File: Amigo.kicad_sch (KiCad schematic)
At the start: 0 parts

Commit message: Power section complete
Schematic Power section
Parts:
- added C1, C2: C, symbol Device:C
- added J1: USB_C_Receptacle_USB2.0_16P, symbol Connector:USB_C_Receptacle_USB2.0_16P
- added J2: Conn_01x02, symbol Connector_Generic:Conn_01x02
- added R1, R2: 5.1k, symbol Device:R
- added R3: 1.2k, symbol Device:R
- added R4, R5: 100k, symbol Device:R
- added U1: TP4056-42-ESOP8, Package_SO:SOIC-8-1EP_3.9x4.9mm_P1.27mm_EP2.41x3.3mm_ThermalVias, symbol Battery_Management:TP4056-42-ESOP8
- added U2: AP2112K-3.3, Package_TO_SOT_SMD:SOT-23-5, symbol Regulator_Linear:AP2112K-3.3
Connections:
- new net +3V3: C2.1, U2.5 (VOUT)
- new net BAT+: C1.1, J2.1 (Pin_1), R4.1, U1.5 (BAT), U2.1 (VIN), U2.3 (EN)
- new net BAT_SENSE: R4.2, R5.1
- new net GND: C1.2, C2.2, J1.A1 (GND), J1.A12 (GND), J1.B1 (GND), J1.B12 (GND), J1.SH (SHIELD), J2.2 (Pin_2), R1.2, R2.2, R3.2, R5.2, U2.2 (GND)
- new net TP4_PROG: R3.1, U1.2 (PROG)
- new net USB_CC1: J1.A5 (CC1), R1.1
- new net USB_CC2: J1.B5 (CC2), R2.1
- new net VBUS_5V: J1.A4 (VBUS), J1.A9 (VBUS), J1.B4 (VBUS), J1.B9 (VBUS), U1.4 (V_{CC})

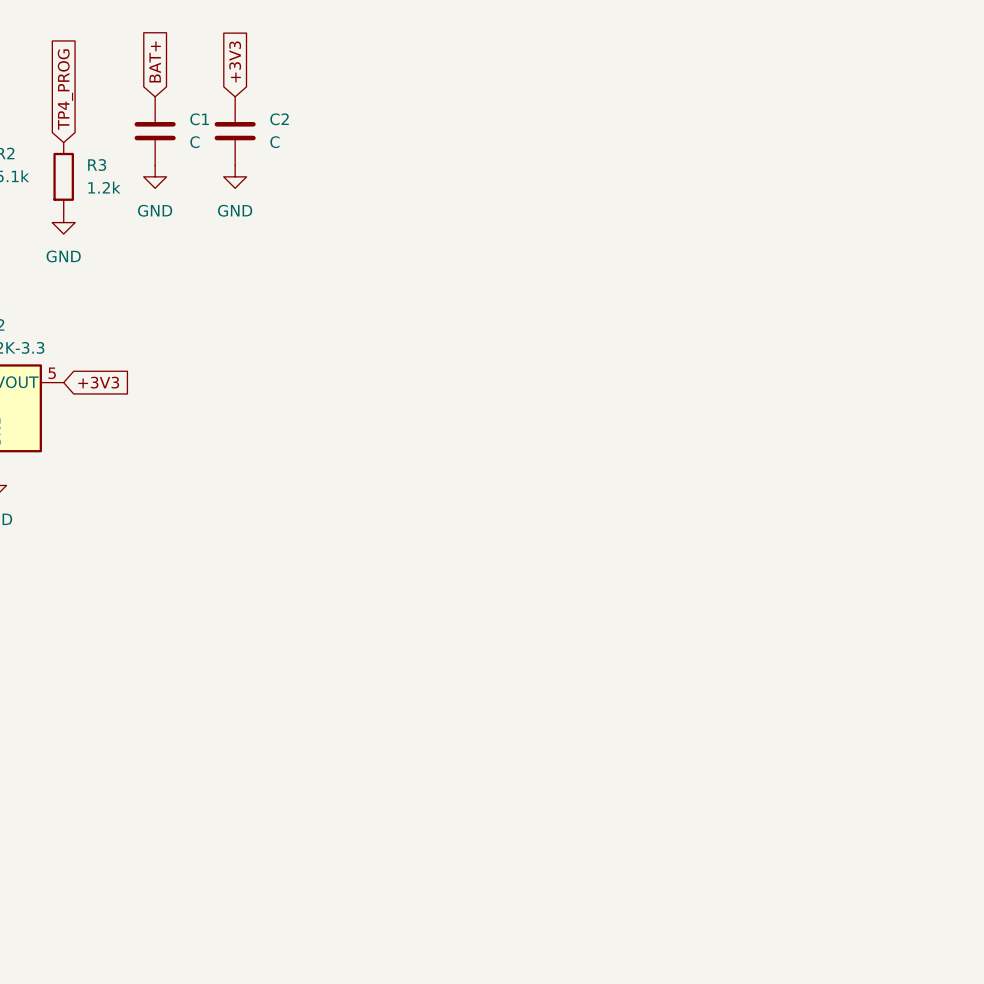
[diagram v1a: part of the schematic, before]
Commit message: Wired up ESP board with all the stuff
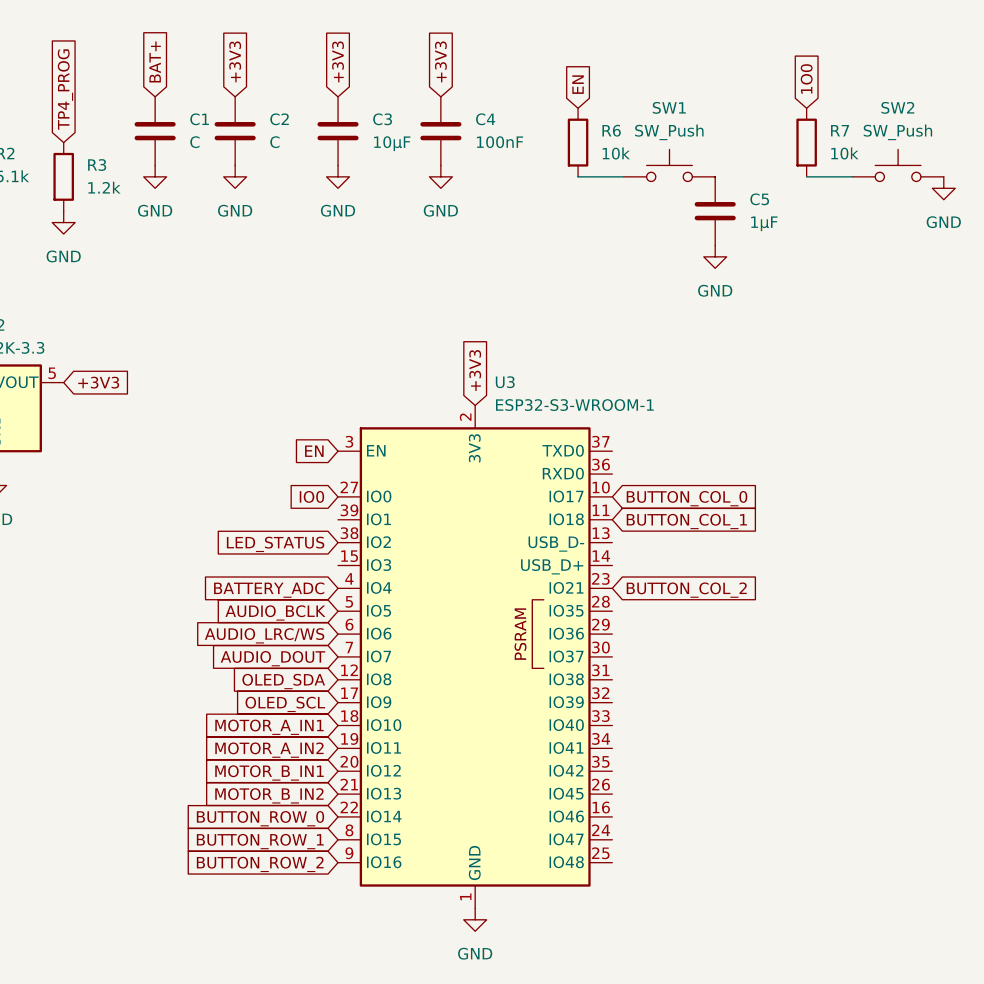
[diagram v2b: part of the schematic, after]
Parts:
- added C3: 10µF, symbol Device:C
- added C4: 100nF, symbol Device:C
- added C5: 1µF, symbol Device:C
- added R6, R7: 10k, symbol Device:R
- added SW1, SW2: SW_Push, symbol Switch:SW_Push
- added U3: ESP32-S3-WROOM-1, RF_Module:ESP32-S3-WROOM-1, symbol RF_Module:ESP32-S3-WROOM-1
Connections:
- net +3V3: now also C3.1, C4.1, U3.2 (3V3)
- net GND: now also C3.2, C4.2, C5.2, SW2.2, U3.1 (GND), U3.40 (GND), U3.41 (GND)
- new net: R6.2, SW1.1
- new net: C5.1, SW1.2
- new net: R7.2, SW2.1
- new net 1O0: R7.1
- new net AUDIO_BCLK: U3.5 (IO5)
- new net AUDIO_DOUT: U3.7 (IO7)
- new net AUDIO_LRC/WS: U3.6 (IO6)
- new net BATTERY_ADC: U3.4 (IO4)
- new net BUTTON_COL_0: U3.10 (IO17)
- new net BUTTON_COL_1: U3.11 (IO18)
- new net BUTTON_COL_2: U3.23 (IO21)
- new net BUTTON_ROW_0: U3.22 (IO14)
- new net BUTTON_ROW_1: U3.8 (IO15)
- new net BUTTON_ROW_2: U3.9 (IO16)
- new net EN: R6.1, U3.3 (EN)
- new net IO0: U3.27 (IO0)
- new net LED_STATUS: U3.38 (IO2)
- new net MOTOR_A_IN1: U3.18 (IO10)
- new net MOTOR_A_IN2: U3.19 (IO11)
- new net MOTOR_B_IN1: U3.20 (IO12)
- new net MOTOR_B_IN2: U3.21 (IO13)
- new net OLED_SCL: U3.17 (IO9)
- new net OLED_SDA: U3.12 (IO8)

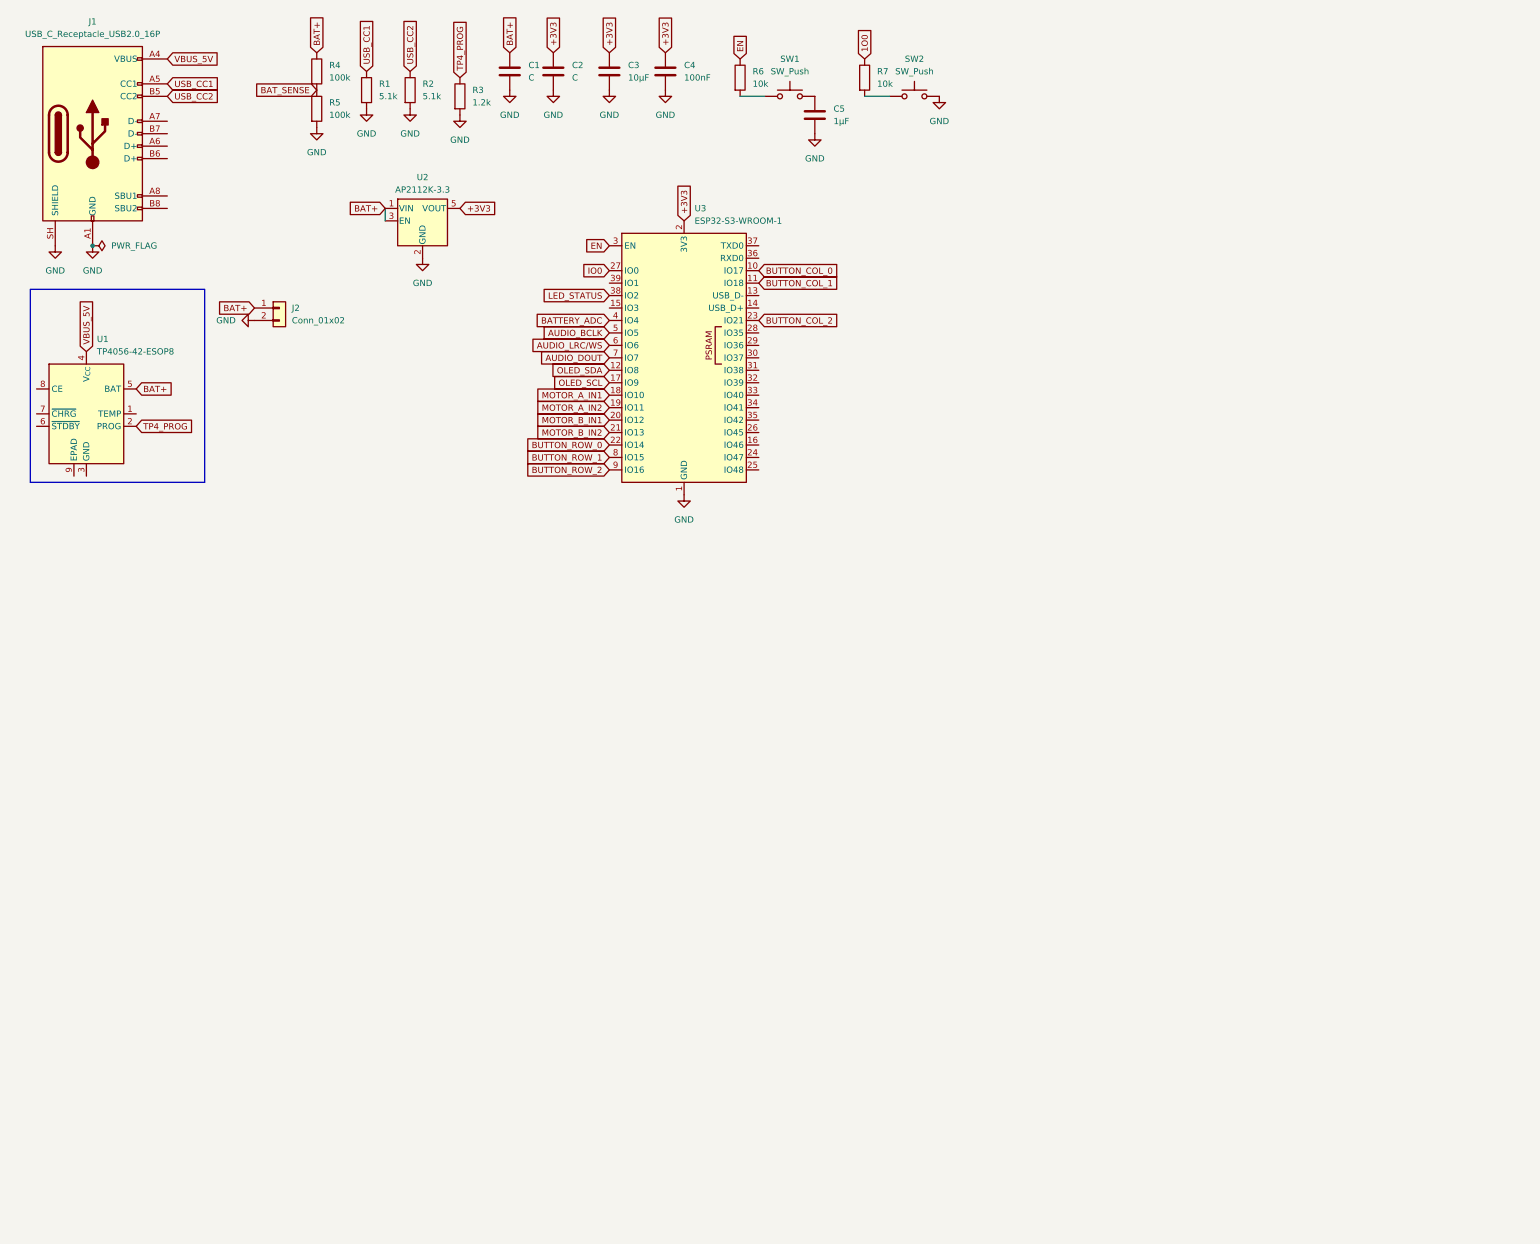
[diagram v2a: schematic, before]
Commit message: Finished wiring audio amp in schematic
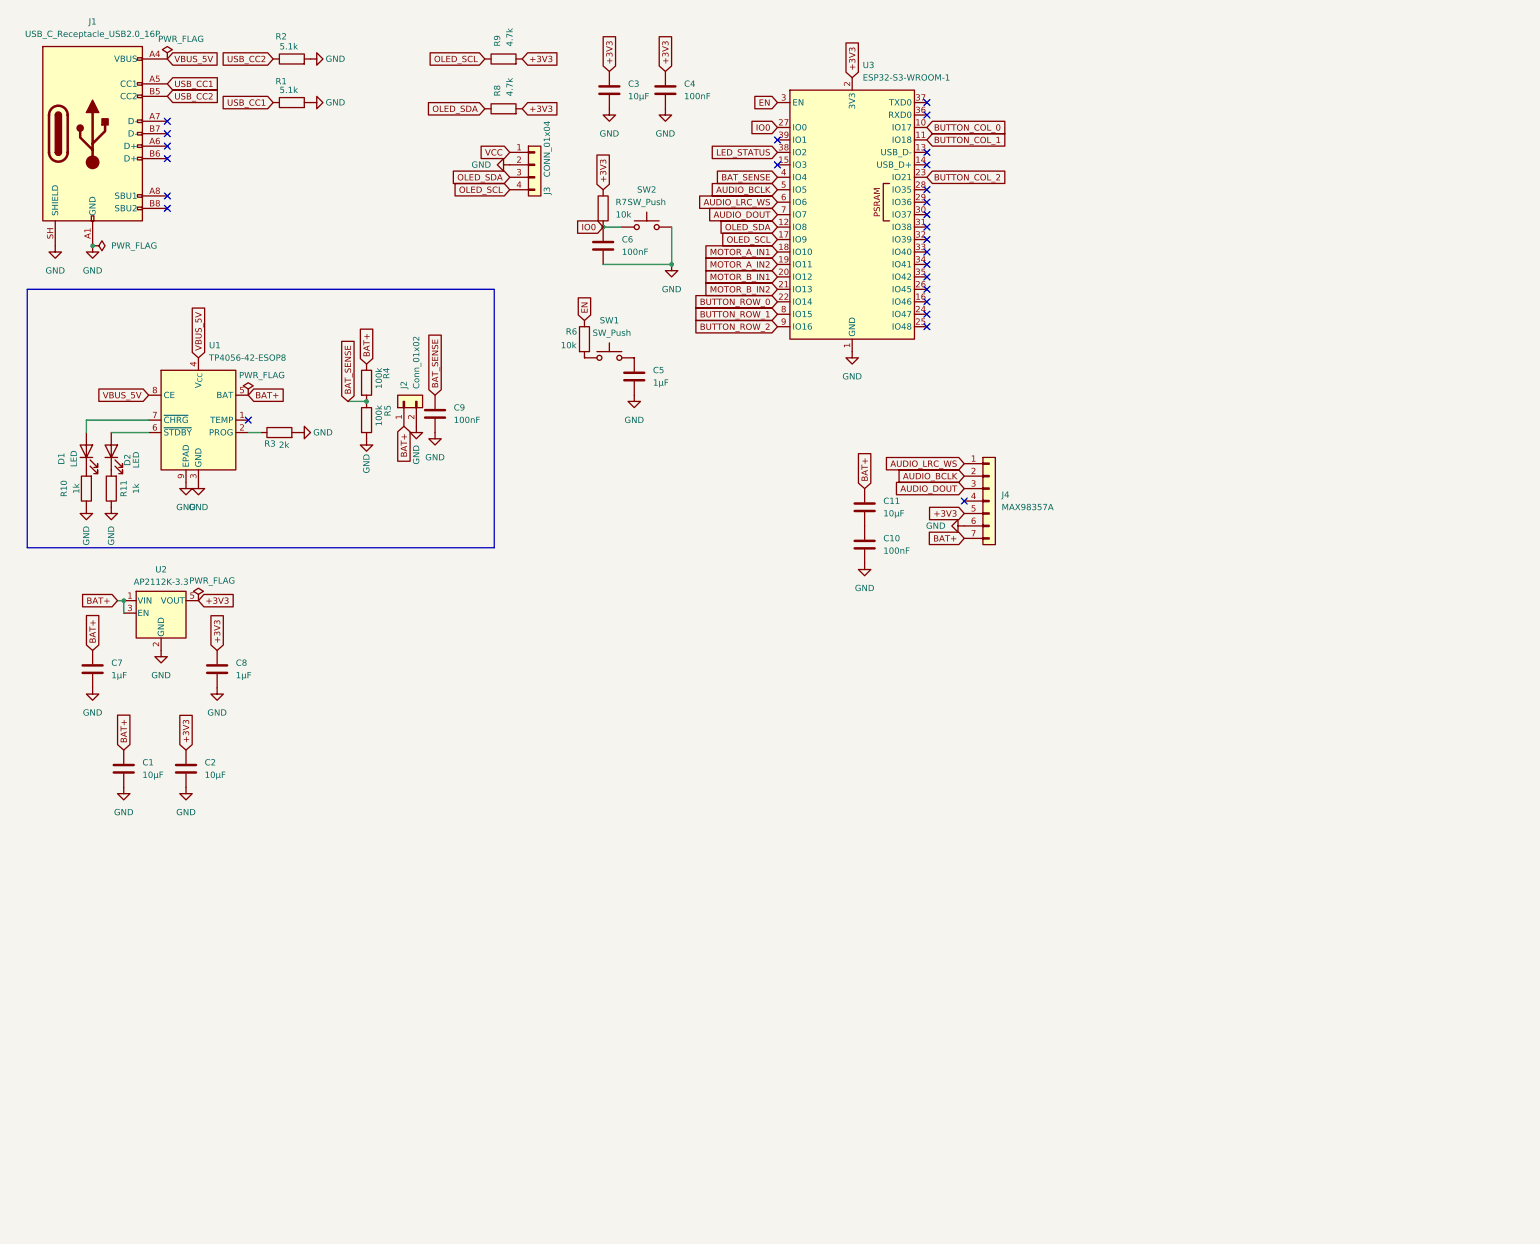
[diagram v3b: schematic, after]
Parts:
- added C10, C6, C9: 100nF, symbol Device:C
- added C11: 10µF, symbol Device:C
- added C7, C8: 1µF, symbol Device:C
- added D1, D2: LED, symbol Device:LED
- added J3: CONN_01x04, symbol Connector_Generic:Conn_01x04
- added J4: MAX98357A, symbol Connector_Generic:Conn_01x07
- added R10, R11: 1k, symbol Device:R
- added R8, R9: 4.7k, symbol Device:R
- C1, C2: value C -> 10µF
- R3: value 1.2k -> 2k
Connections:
- net 1O0 is gone; now on net +3V3: R7.1
- net BATTERY_ADC is gone; now on net BAT_SENSE: U3.4 (IO4)
- net +3V3: now also C8.1, J4.5 (Pin_5), R8.2, R9.2
- net AUDIO_BCLK: now also J4.2 (Pin_2)
- net AUDIO_DOUT: now also J4.3 (Pin_3)
- net BAT+: now also C11.1, C7.1, J4.7 (Pin_7)
- net BAT_SENSE: now also C9.1
- net GND: now also U1.3 (GND), U1.9 (EPAD), C10.2, C6.2, C7.2, C8.2, C9.2, J3.2 (Pin_2), J4.6 (Pin_6), R10.1, R11.1
- net IO0: now also R7.2, SW2.1, C6.1
- net OLED_SCL: now also J3.4 (Pin_4), R9.1
- net OLED_SDA: now also J3.3 (Pin_3), R8.1
- net VBUS_5V: now also U1.8 (CE)
- net at U1.6 (~{STDBY}): now also D2.2 (A)
- net at U1.7 (~{CHRG}): now also D1.2 (A)
- net AUDIO_LRC/WS renamed AUDIO_LRC_WS
- net AUDIO_LRC_WS: now also J4.1 (Pin_1)
- net TP4_PROG: no longer names the net of R3.1, U1.2 (PROG)
- new net: D1.1 (K), R10.2
- new net: D2.1 (K), R11.2
- new net: C10.1, C11.2
- new net VCC: J3.1 (Pin_1)
- no-connect marks 0 -> 26
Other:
- moved on the sheet: C1, C2, C3, C4, C5, J2, R1, R2, R3, R4, R5, R6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

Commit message: Finished wiring motor controller in schematic
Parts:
- added C12: 100nF, symbol Device:C
- added C13: 10µF, symbol Device:C
- added J5: DRV8833, symbol Connector_Generic:Conn_01x08
- J3: value CONN_01x04 -> SH1106 OLED
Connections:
- net +3V3: now also J5.3 (Pin_3), J5.4 (Pin_4)
- net BAT+: now also C12.1, C13.1, J5.1 (Pin_1)
- net GND: now also C12.2, C13.2, J5.2 (Pin_2)
- net MOTOR_A_IN1: now also J5.5 (Pin_5)
- net MOTOR_A_IN2: now also J5.6 (Pin_6)
- net MOTOR_B_IN1: now also J5.7 (Pin_7)
- net MOTOR_B_IN2: now also J5.8 (Pin_8)
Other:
- moved on the sheet: C10, C11, C5, J3, J4, R6, R8, R9, SW1

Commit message: Finished button matrix in schematic. Ready to move on to PCB
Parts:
- added D10, D11, D12, D4, D5, D6, D7, D8, D9: 1N4148W, Diode_SMD:D_SOD-123, symbol Diode:1N4148W
- added D3: LED, symbol Device:LED
- added R12: 1k, symbol Device:R
- added R13, R14, R15: 10k, symbol Device:R
- added SW10, SW11, SW3, SW4, SW5, SW6, SW7, SW8, SW9: SW_Push, symbol Switch:SW_Push
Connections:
- net VCC is gone; now on net +3V3: J3.1 (Pin_1)
- net +3V3: now also R13.1, R14.1, R15.1
- net BUTTON_COL_0: now also D10.2 (A), D4.2 (A), D7.2 (A), R13.2
- net BUTTON_COL_1: now also D11.2 (A), D5.2 (A), D8.2 (A), R14.2
- net BUTTON_COL_2: now also D12.2 (A), D6.2 (A), D9.2 (A), R15.2
- net BUTTON_ROW_0: now also SW3.2, SW4.2, SW5.2
- net BUTTON_ROW_1: now also SW6.2, SW7.2, SW8.2
- net BUTTON_ROW_2: now also SW10.2, SW11.2, SW9.2
- net GND: now also D3.2 (A)
- net LED_STATUS: now also R12.2
- new net: D4.1 (K), SW3.1
- new net: D5.1 (K), SW4.1
- new net: D3.1 (K), R12.1
- new net: D6.1 (K), SW5.1
- new net: D11.1 (K), SW10.1
- new net: D9.1 (K), SW8.1
- new net: D8.1 (K), SW7.1
- new net: D7.1 (K), SW6.1
- new net: D12.1 (K), SW11.1
- new net: D10.1 (K), SW9.1
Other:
- moved on the sheet: R9

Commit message: PCB updating and annotating
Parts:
- removed D10, D11, D12, D4, D5, D6, D7, D8, D9: 1N4148W, Diode_SMD:D_SOD-123, symbol Diode:1N4148W
- removed R13, R14, R15: 10k, symbol Device:R
- removed SW10, SW11, SW3, SW4, SW5, SW6, SW7, SW8, SW9: SW_Push, symbol Switch:SW_Push
- added J6: ButtonRibbonConnector, Connector_PinHeader_2.54mm:PinHeader_1x08_P2.54mm_Vertical, symbol Connector_Generic:Conn_01x08
- C1, C10, C11, C12, C2, C3, C4, C5, C6, C7, C8, C9: footprint (none) -> Capacitor_SMD:C_0603_1608Metric
- C13: footprint (none) -> Capacitor_SMD:C_0805_2012Metric
- D1, D2, D3: footprint (none) -> LED_SMD:LED_0805_2012Metric
- J1: footprint (none) -> Connector_USB:USB_C_Receptacle_GCT_USB4085
- J2: footprint (none) -> Connector_JST:JST_PH_S2B-PH-K_1x02_P2.00mm_Horizontal
- J3: footprint (none) -> Connector_PinHeader_2.54mm:PinHeader_1x04_P2.54mm_Vertical
- J4: footprint (none) -> Connector_PinHeader_2.54mm:PinHeader_1x07_P2.54mm_Vertical
- J5: footprint (none) -> Connector_PinHeader_2.54mm:PinHeader_1x08_P2.54mm_Vertical
- R1, R10, R11, R12, R2, R3, R4, R5, R6, R7, R8, R9: footprint (none) -> Resistor_SMD:R_0603_1608Metric
- SW1, SW2: footprint (none) -> Button_Switch_SMD:SW_SPST_TL3342
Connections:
- net +3V3: now also J6.1 (Pin_1)
- net BUTTON_COL_0: now also J6.6 (Pin_6)
- net BUTTON_COL_1: now also J6.7 (Pin_7)
- net BUTTON_COL_2: now also J6.8 (Pin_8)
- net BUTTON_ROW_0: now also J6.3 (Pin_3)
- net BUTTON_ROW_1: now also J6.4 (Pin_4)
- net BUTTON_ROW_2: now also J6.5 (Pin_5)
- net GND: now also J6.2 (Pin_2)

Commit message: Found out why there is a discrepancy with two main board files. The real one is in the Main Board folder
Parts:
- removed C1, C11, C2, C3: 10µF, Capacitor_SMD:C_0603_1608Metric, symbol Device:C
- removed C10, C12, C4, C6, C9: 100nF, Capacitor_SMD:C_0603_1608Metric, symbol Device:C
- removed C13: 10µF, Capacitor_SMD:C_0805_2012Metric, symbol Device:C
- removed C5, C7, C8: 1µF, Capacitor_SMD:C_0603_1608Metric, symbol Device:C
- removed D1, D2, D3: LED, LED_SMD:LED_0805_2012Metric, symbol Device:LED
- removed J1: USB_C_Receptacle_USB2.0_16P, Connector_USB:USB_C_Receptacle_GCT_USB4085, symbol Connector:USB_C_Receptacle_USB2.0_16P
- removed J2: Conn_01x02, Connector_JST:JST_PH_S2B-PH-K_1x02_P2.00mm_Horizontal, symbol Connector_Generic:Conn_01x02
- removed J3: SH1106 OLED, Connector_PinHeader_2.54mm:PinHeader_1x04_P2.54mm_Vertical, symbol Connector_Generic:Conn_01x04
- removed J4: MAX98357A, Connector_PinHeader_2.54mm:PinHeader_1x07_P2.54mm_Vertical, symbol Connector_Generic:Conn_01x07
- removed J5: DRV8833, Connector_PinHeader_2.54mm:PinHeader_1x08_P2.54mm_Vertical, symbol Connector_Generic:Conn_01x08
- removed J6: ButtonRibbonConnector, Connector_PinHeader_2.54mm:PinHeader_1x08_P2.54mm_Vertical, symbol Connector_Generic:Conn_01x08
- removed R1, R2: 5.1k, Resistor_SMD:R_0603_1608Metric, symbol Device:R
- removed R10, R11, R12: 1k, Resistor_SMD:R_0603_1608Metric, symbol Device:R
- removed R3: 2k, Resistor_SMD:R_0603_1608Metric, symbol Device:R
- removed R4, R5: 100k, Resistor_SMD:R_0603_1608Metric, symbol Device:R
- removed R6, R7: 10k, Resistor_SMD:R_0603_1608Metric, symbol Device:R
- removed R8, R9: 4.7k, Resistor_SMD:R_0603_1608Metric, symbol Device:R
- removed SW1, SW2: SW_Push, Button_Switch_SMD:SW_SPST_TL3342, symbol Switch:SW_Push
- removed U1: TP4056-42-ESOP8, Package_SO:SOIC-8-1EP_3.9x4.9mm_P1.27mm_EP2.41x3.3mm_ThermalVias, symbol Battery_Management:TP4056-42-ESOP8
- removed U2: AP2112K-3.3, Package_TO_SOT_SMD:SOT-23-5, symbol Regulator_Linear:AP2112K-3.3
- removed U3: ESP32-S3-WROOM-1, RF_Module:ESP32-S3-WROOM-1, symbol RF_Module:ESP32-S3-WROOM-1
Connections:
- no-connect marks 26 -> 0
